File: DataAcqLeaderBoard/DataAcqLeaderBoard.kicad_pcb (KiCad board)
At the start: 2 copper layers, 71 parts, among them J2 PER_CAN, J3 PER_PWR, J4 CCAN_IN, J5 CCAN_OUT, J6 PWR_IN, SW1 RF_RESET, SW2 RF_COM, SW3 LTE_RESET, SW4 GPS_RESET, U1 PA1616S_GPS, X1 DigiXBeeRX900Micro, X2 DigiXBee3LTECat4

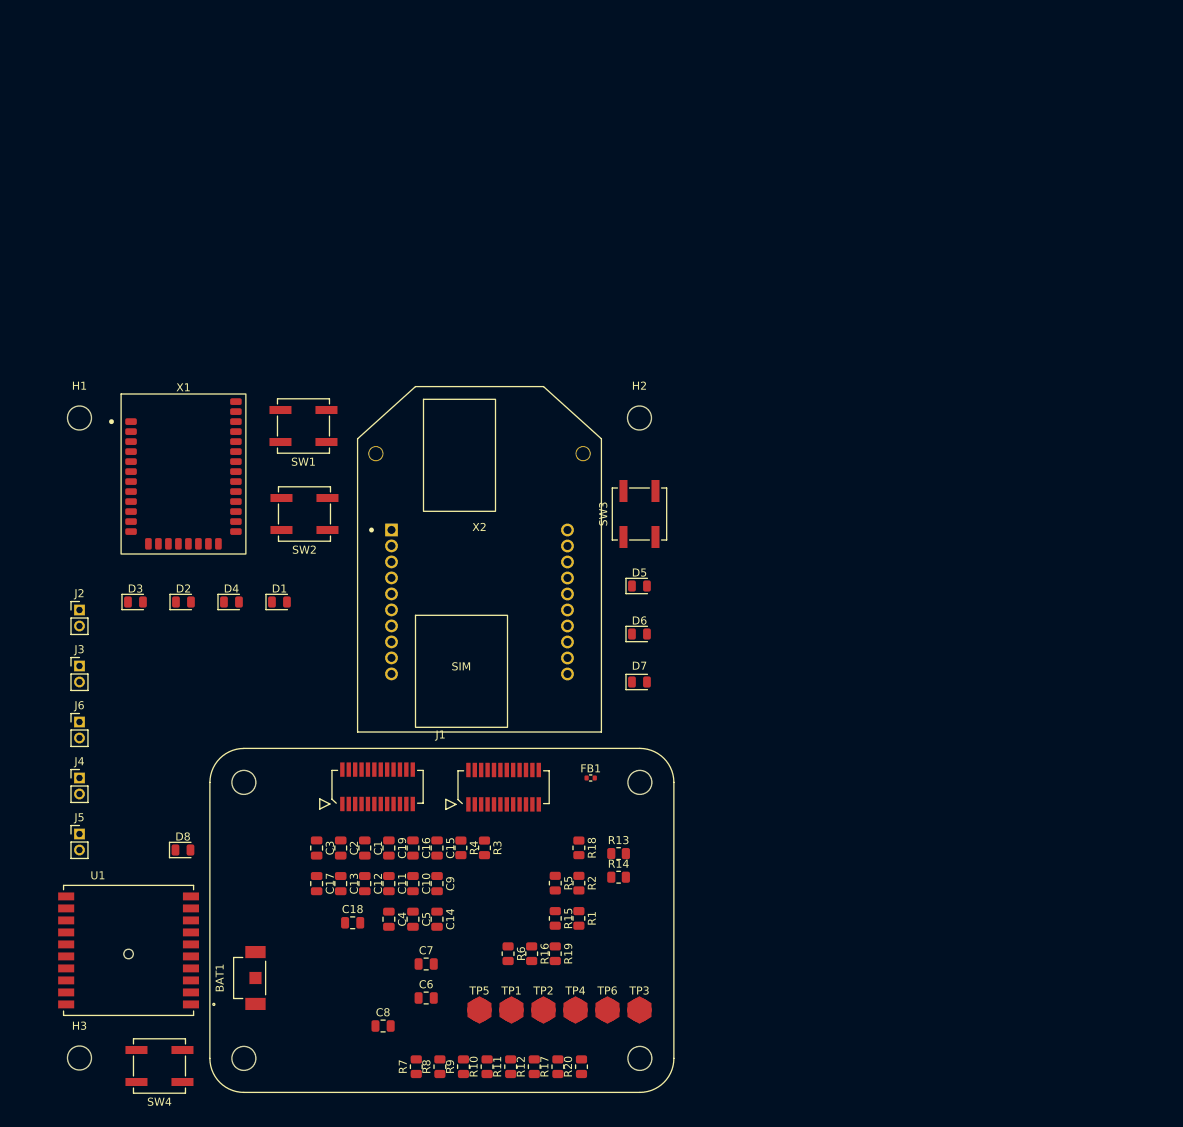
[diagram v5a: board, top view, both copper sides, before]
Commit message: Completed first draft of layout
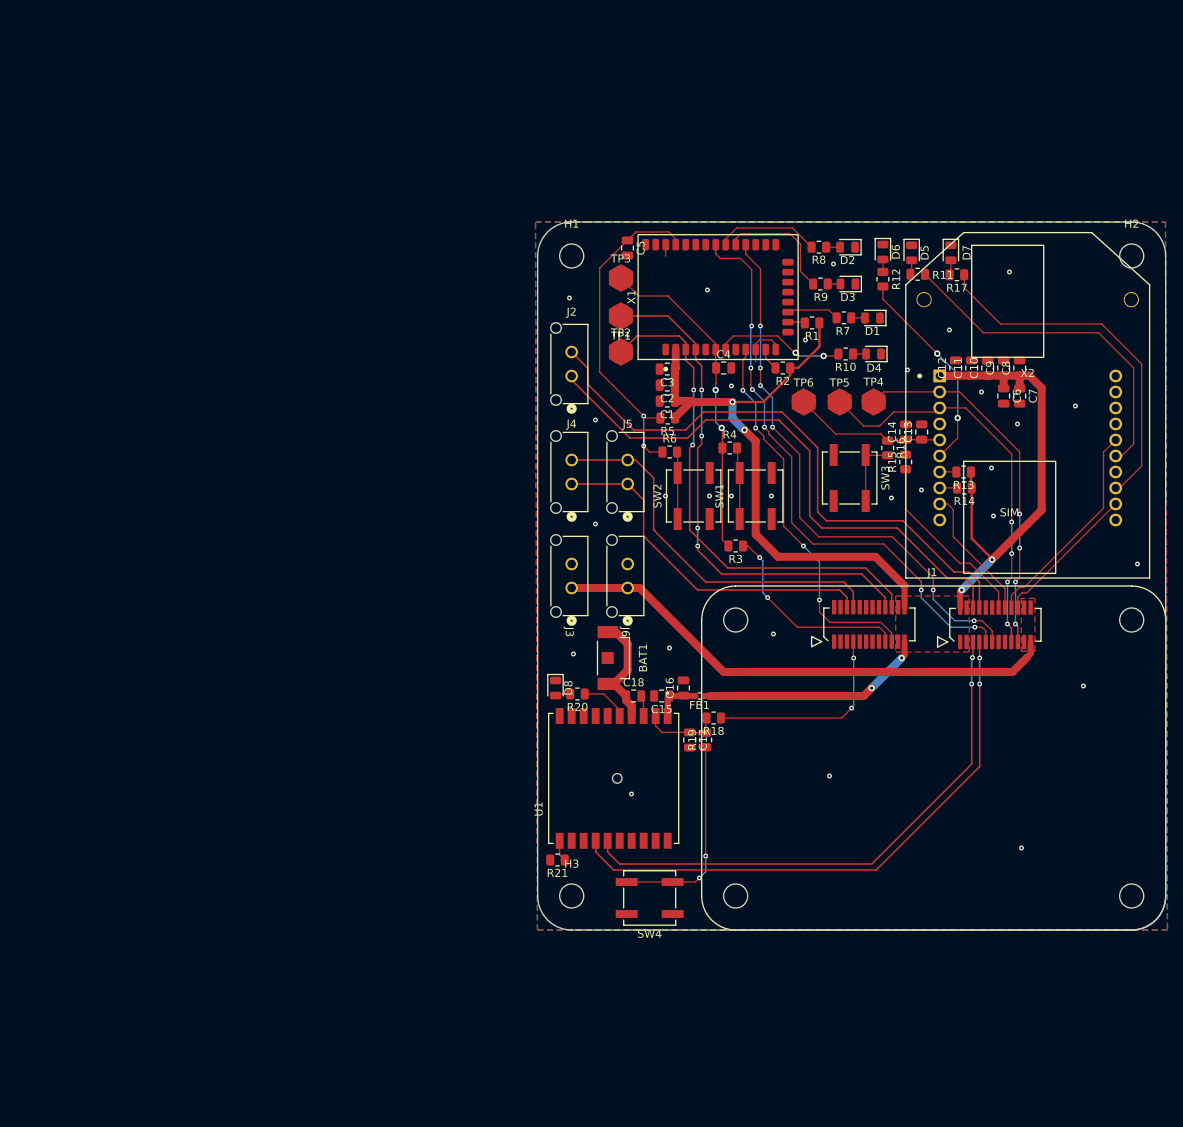
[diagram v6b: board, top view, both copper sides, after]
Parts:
- removed C19: 0.1u, Capacitor_SMD:C_0805_2012Metric
- added R21: 10k, Resistor_SMD:R_0805_2012Metric, F.Cu at (149.8, 135.2)
- J2, J3, J4, J5, J6: footprint Connector_PinHeader_2.00mm:PinHeader_1x02_P2.00mm_Vertical -> DataAcqLeaderBoard-Footprints:CONN_SD-43650-006_02_MOL
- moved C8 114.4 mm to (207.5, 73.8), turned to 90 degrees
- moved R8 112.9 mm to (182.4, 58.6), turned to 0 degrees
- moved R11 111.4 mm to (194.8, 62.0), turned to 180 degrees
- moved R17 110.8 mm to (199.7, 62.1), turned to 180 degrees
- moved R7 107.8 mm to (185.6, 67.5), turned to 0 degrees
- moved R12 107.7 mm to (190.4, 62.6)
- moved R9 107.5 mm to (182.6, 63.2), turned to 0 degrees
- moved C6 104.3 mm to (205.5, 77.2), turned to -90 degrees
- moved C7 102.7 mm to (207.5, 77.2), turned to -90 degrees
- moved R10 99.7 mm to (185.8, 72.0), turned to 0 degrees
- moved C12 98.0 mm to (199.5, 73.8), turned to 90 degrees
- moved D3 97.5 mm to (186.1, 63.2), turned to 180 degrees
- moved C11 97.3 mm to (201.5, 73.8), turned to 90 degrees
- moved C10 96.5 mm to (203.5, 73.8), turned to 90 degrees
- moved C9 95.8 mm to (205.5, 73.8), turned to 90 degrees
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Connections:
- net /GPS_CoinBattery_Supply renamed /+3.3V_GPS_BAT
- net /GPS_VCC renamed /+3.3V_GPS
- net Net-(D1-A) renamed /RF_D1
- net Net-(D2-A) renamed /RF_D2
- net Net-(D3-A) renamed /RF_D3
- net Net-(D4-A) renamed /RF_D4
- net Net-(D5-A) renamed /LTE_D5
- net Net-(D6-A) renamed /LTE_D6
- net Net-(D7-A) renamed /LTE_D7
- net Net-(D8-A) renamed /GPS_D8
- net Net-(R16-Pad2) renamed /LTE_SW3
- net Net-(R19-Pad1) renamed /GPS_SW4
- net Net-(R4-Pad2) renamed /RF_SW1
- net Net-(R6-Pad2) renamed /RF_SW2
- net Net-(X1-SPI_N_SSEL/DIO17) renamed /RF_SPI_OFF
- net Net-(X2-PWM1/DIO11/USB_D+/I2C_SDA) renamed /LTE_D+_OFF
- net Net-(X2-USB_D-) renamed /LTE_D-_OFF
- J1 pad 11: /RF_NRESET_MCU -> /RF_NCTS
- J1 pad 14: /LTE_NCTS -> /LTE_NRESET_MCU
- J1 pad 16: /LTE_NRTS -> /LTE_NDTR/SLEEP_RQ
- J1 pad 18: /LTE_NRESET_MCU -> /LTE_NRTS
- J1 pad 20: /LTE_NDTR/SLEEP_RQ -> /LTE_NCTS
- J1 pad 31: /GPS_NRESET -> /GPS_NRESET_MCU
- J1 pad 41: /RF_NRTS -> /RF_NRESET_MCU
- J1 pad 43: /RF_NCTS -> /RF_SLEEP
- J1 pad 9: /RF_SLEEP -> /RF_NRTS
- R18 pad 1: /GPS_NRESET -> /GPS_NRESET_MCU
- U1 pad 11: Net-(U1-EX_ANT) -> /GPS_EXT_OFF
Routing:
- net +3.3V: track 0.00 -> 164.9 mm, vias 0 -> 6
- net /CAN_PERF_L: track 0.00 -> 73.8 mm
- net /RF_NRTS: track 0.00 -> 72.7 mm, vias 0 -> 6
- net /GPS_I2C_SCL: track 0.00 -> 71.3 mm, vias 0 -> 2
- net /CAN_PERF_H: track 0.00 -> 70.7 mm
- net /RF_NCTS: track 0.00 -> 69.8 mm, vias 0 -> 6
- net /GPS_I2C_SDA: track 0.00 -> 68.0 mm, vias 0 -> 2
- net /RF_UART_TX: track 0.00 -> 64.3 mm, vias 0 -> 2
- net /RF_UART_RX: track 0.00 -> 64.2 mm, vias 0 -> 4
- net +12V: track 0.00 -> 64.1 mm
- net /LTE_UART_RX: track 0.00 -> 50.0 mm, vias 0 -> 4
- net /RF_SLEEP: track 0.00 -> 48.5 mm, vias 0 -> 4
- net /CAN_CAR_L: track 0.00 -> 47.8 mm
- net /LTE_UART_TX: track 0.00 -> 46.3 mm, vias 0 -> 4
- net /LTE_STATUS_ON: track 0.00 -> 44.9 mm
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- added copper zone on F.Cu, net +12V
- added copper zone on F.Cu, net +3.3V
- added copper zone on B.Cu, net GND
- added copper zone on F.Cu, net GND
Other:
- board outline added: 78.5 x 88.5 mm

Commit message: Updated Schematic, finished first rev of Layout
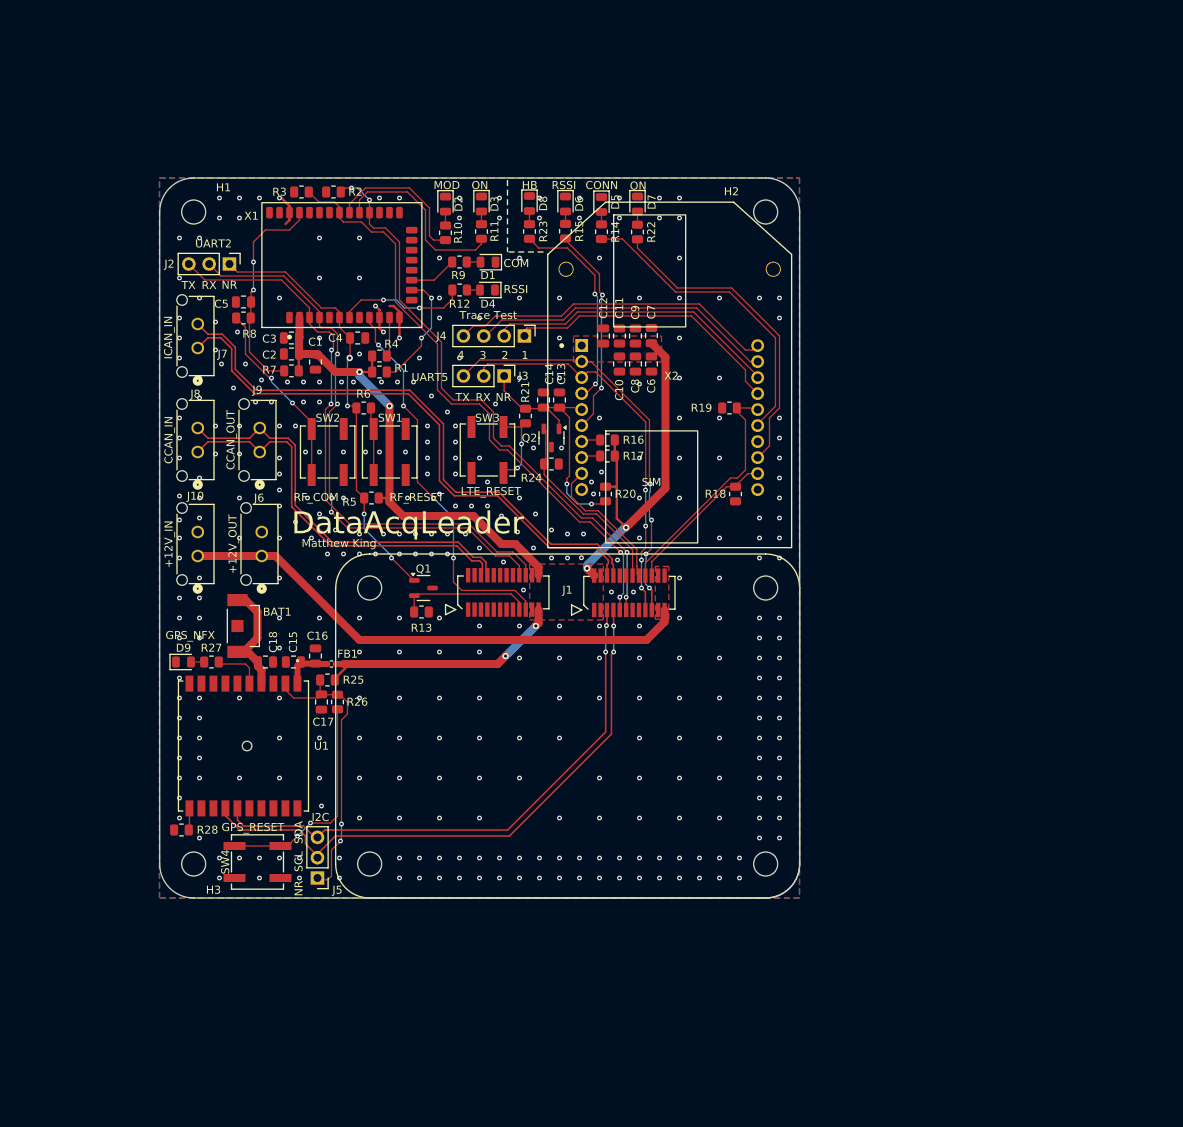
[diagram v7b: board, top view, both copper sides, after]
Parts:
- removed TP1: RF_UART_RX, UTSVT_Special:TestPoint_HEX_3mmID
- removed TP2: RF_UART_TX, UTSVT_Special:TestPoint_HEX_3mmID
- removed TP3: RF_NREST, UTSVT_Special:TestPoint_HEX_3mmID
- removed TP4: LTE_UART_TX, UTSVT_Special:TestPoint_HEX_3mmID
- removed TP5: LTE_UART_RX, UTSVT_Special:TestPoint_HEX_3mmID
- removed TP6: LTE_NRESET, UTSVT_Special:TestPoint_HEX_3mmID
- added D8: LTE_HeartBeat, LED_SMD:LED_0805_2012Metric, F.Cu at (146.2, 53.2)
- added J6: PWR_OUT, DataAcqLeaderBoard-Footprints:CONN_SD-43650-006_02_MOL, F.Cu at (112.5, 95.8)
- added J7: ICAN_IN, DataAcqLeaderBoard-Footprints:CONN_SD-43650-006_02_MOL, F.Cu at (104.5, 69.8)
- added J8: CCAN_IN, DataAcqLeaderBoard-Footprints:CONN_SD-43650-006_02_MOL, F.Cu at (104.5, 82.8)
- added J9: CCAN_OUT, DataAcqLeaderBoard-Footprints:CONN_SD-43650-006_02_MOL, F.Cu at (112.2, 82.8)
- added Q1: NMOS, Package_TO_SOT_SMD:SOT-23-3, F.Cu at (133.0, 101.2)
- added Q2: NMOS, Package_TO_SOT_SMD:SOT-23-3, F.Cu at (149.0, 82.5)
- added R13: 10k, Resistor_SMD:R_0805_2012Metric, F.Cu at (132.8, 104.2)
- added R18: 10k, Resistor_SMD:R_0805_2012Metric, F.Cu at (172.0, 89.5)
- added R19: 10k, Resistor_SMD:R_0805_2012Metric, F.Cu at (171.2, 78.8)
- added R2: 10k, Resistor_SMD:R_0805_2012Metric, F.Cu at (121.8, 51.8)
- added R23: 1k, Resistor_SMD:R_0805_2012Metric, F.Cu at (146.2, 56.7)
- added R24: 10k, Resistor_SMD:R_0805_2012Metric, F.Cu at (149.0, 85.8)
- added R3: 10k, Resistor_SMD:R_0805_2012Metric, F.Cu at (117.8, 51.8)
- J2: value PER_CAN -> RF_UART; footprint DataAcqLeaderBoard-Footprints:CONN_SD-43650-006_02_MOL -> Connector_PinHeader_2.54mm:PinHeader_1x03_P2.54mm_Vertical
- J3: value PER_PWR -> LTE_UART; footprint DataAcqLeaderBoard-Footprints:CONN_SD-43650-006_02_MOL -> Connector_PinHeader_2.54mm:PinHeader_1x03_P2.54mm_Vertical
- J4: value CCAN_IN -> LTE_Trace; footprint DataAcqLeaderBoard-Footprints:CONN_SD-43650-006_02_MOL -> Connector_PinHeader_2.54mm:PinHeader_1x04_P2.54mm_Vertical
- J5: value CCAN_OUT -> GPS_I2C; footprint DataAcqLeaderBoard-Footprints:CONN_SD-43650-006_02_MOL -> Connector_PinHeader_2.54mm:PinHeader_1x03_P2.54mm_Vertical
- R10: renamed from R8; value 700 -> 1k
- R11: renamed from R9; value 700 -> 1k
- R12: renamed from R10; value 700 -> 1k
- R14: renamed from R11; value 700 -> 1k
- R15: renamed from R12; value 700 -> 1k
- R21: renamed from R16; value 700 -> 1k
- R22: renamed from R17; value 700 -> 1k
- R26: renamed from R19; value 700 -> 1k
- R27: renamed from R20; value 700 -> 1k
- R6: renamed from R4; value 700 -> 1k
- R8: renamed from R6; value 700 -> 1k
- R9: renamed from R7; value 700 -> 1k
- moved J5 63.7 mm to (119.8, 137.5), turned to 180 degrees
- moved R8 55.8 mm to (110.5, 67.5), turned to 180 degrees
- moved R1 54.4 mm to (127.5, 74.2), turned to 0 degrees
- moved J10 53.9 mm to (104.5, 95.8)
- moved D2 50.6 mm to (135.8, 53.3), turned to -90 degrees
- moved R4 50.4 mm to (127.5, 72.2), turned to 0 degrees
- moved SW4 49.2 mm to (112.2, 135.5)
- moved D4 48.9 mm to (141.0, 64.0)
- moved R12 48.9 mm to (137.5, 64.0)
- moved D1 48.6 mm to (141.1, 60.5)
- moved R9 48.6 mm to (137.5, 60.5)
- moved R25 48.5 mm to (121.0, 112.8), turned to 0 degrees
- moved C5 48.5 mm to (110.5, 65.5), turned to 180 degrees
- moved C8 48.0 mm to (159.5, 73.2), turned to -90 degrees
- moved H1 47.6 mm to (104.3, 54.2)
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- renumbered D8 to D9, J6 to J10, R13 to R16, R14 to R17, R15 to R20, R18 to R25, R21 to R28, R2 to R4, R3 to R5, R5 to R7
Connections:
- net /GPS_D8 renamed /GPS_D9
- J1 pad 30: /CAN_CAR_H -> /CAN_CAR_+
- J1 pad 31: /GPS_NRESET_MCU -> unconnected-(J1B-ADC1_IN10-Pad31)
- J1 pad 32: /CAN_CAR_L -> /CAN_CAR_-
- J1 pad 6: /CAN_PERF_H -> /CAN_PERF_+
- J1 pad 8: /CAN_PERF_L -> /CAN_PERF_-
- J2 pad 1: /CAN_PERF_H -> /RF_NRESET
- J2 pad 2: /CAN_PERF_L -> /RF_UART_RX
- J3 pad 1: +12V -> /LTE_NRESET
- J3 pad 2: GND -> /LTE_UART_RX
- J4 pad 1: /CAN_CAR_H -> /LTE_Trace1
- J4 pad 2: /CAN_CAR_L -> /LTE_Trace2
- J5 pad 1: /CAN_CAR_H -> /GPS_NRESET
- J5 pad 2: /CAN_CAR_L -> /GPS_I2C_SCL
- R20 pad 1: /LTE_NRESET_MCU -> +3.3V
- R25 pad 1: /GPS_NRESET_MCU -> /GPS_NRESET
- R25 pad 2: /GPS_NRESET -> +3.3V
- R5 pad 1: /RF_NRESET_MCU -> +3.3V
- X2 pad 17: unconnected-(X2-AD3/DIO3/SPI_N_SS/CTS_2-Pad17) -> /LTE_Trace1
- X2 pad 18: unconnected-(X2-AD2/DIO2/SPI_CLK/RTS_2-Pad18) -> /LTE_Trace2
- X2 pad 19: unconnected-(X2-AD1/DIO1/SPI_N_ATTN/I2C_SCL-Pad19) -> /LTE_Trace3
- X2 pad 20: unconnected-(X2-AD0/DIO0-Pad20) -> /LTE_Trace4
- X2 pad 4: unconnected-(X2-DIO12/SPI_MISO/UART_RX2-Pad4) -> /LTE_STATUS_HB
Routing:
- net /CAN_PERF_L: track 73.8 -> 0.00 mm
- net /CAN_PERF_-: track 0.00 -> 72.1 mm
- net /CAN_PERF_+: track 0.00 -> 71.9 mm
- net /CAN_PERF_H: track 70.7 -> 0.00 mm
- net /CAN_CAR_-: track 0.00 -> 50.1 mm
- net /CAN_CAR_+: track 0.00 -> 49.4 mm
- net /CAN_CAR_L: track 47.8 -> 0.00 mm
- net /CAN_CAR_H: track 44.2 -> 0.00 mm
- net /LTE_Trace4: track 0.00 -> 41.0 mm
- net /LTE_Trace3: track 0.00 -> 38.5 mm
- net /LTE_Trace2: track 0.00 -> 36.9 mm
- net /LTE_Trace1: track 0.00 -> 35.6 mm
- net /LTE_STATUS_HB: track 0.00 -> 26.1 mm, vias 0 -> 2
- net /GPS_NRESET: track 10.2 -> 35.9 mm, vias 0 -> 2
- net /GPS_NRESET_MCU: track 25.3 -> 0.00 mm, vias 2 -> 0
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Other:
- board size 78.5 x 88.5 mm -> 80 x 90 mm
- board text added: "+12V_IN"
- board text added: "+12V_OUT"
- board text added: "1"
- board text added: "2"
- board text added: "3"
- board text added: "4"
- board text added: "CCAN_IN"
- board text added: "CCAN_OUT"
- board text added: "COM"
- board text added: "CONN"
- board text added: "DataAcqLeader"
- board text added: "GPS_NFX"
- board text added: "GPS_RESET"
- board text added: "HB"
- board text added: "I2C"
- board text added: "ICAN_IN"
- board text added: "LTE_RESET"
- board text added: "MOD"
- board text added: "Matthew King"
- board text added: "NR"
- board text added: "ON"
- board text added: "RF_COM"
- board text added: "RF_RESET"
- board text added: "RSSI"
- board text added: "RX"
- board text added: "SCL"
- board text added: "SDA"
- board text added: "TX"
- board text added: "Trace Test"
- board text added: "UART2"
- board text added: "UART5"

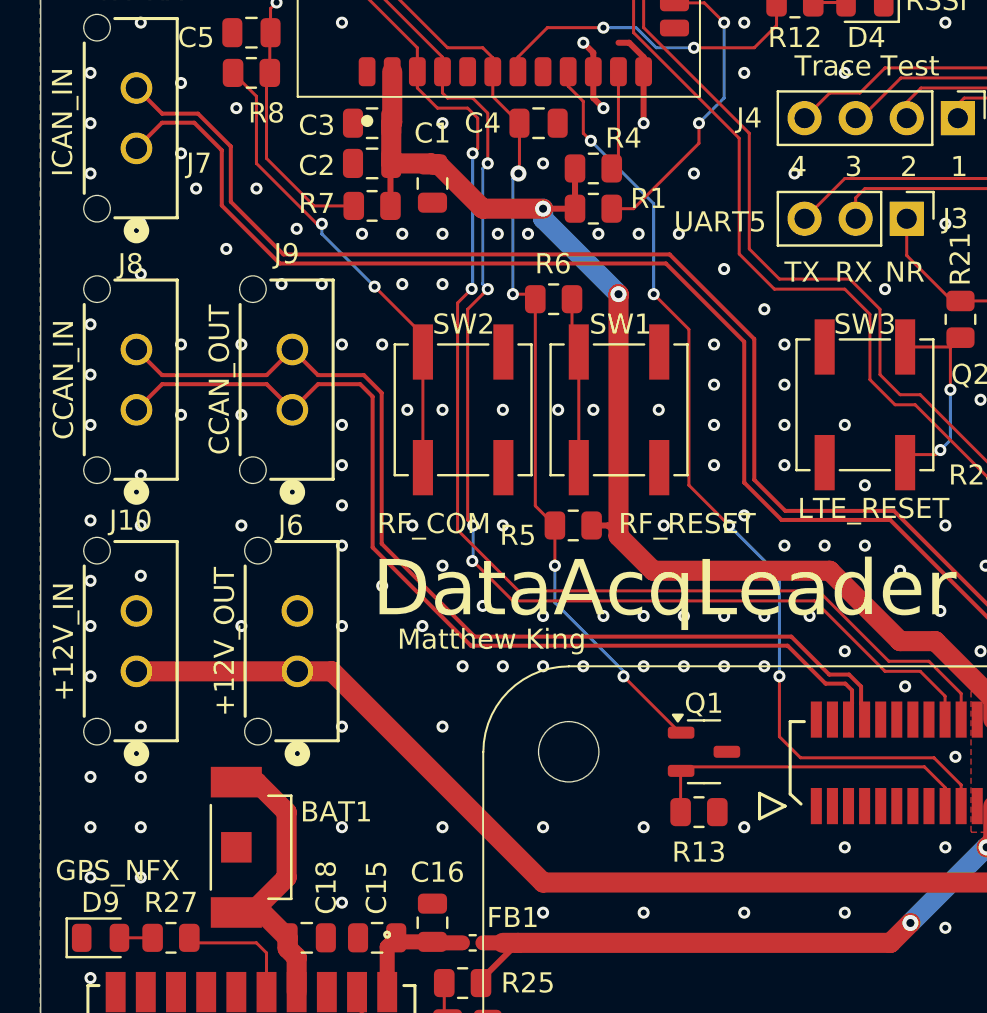
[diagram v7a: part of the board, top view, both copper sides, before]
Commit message: Added README, added PCB dimensions
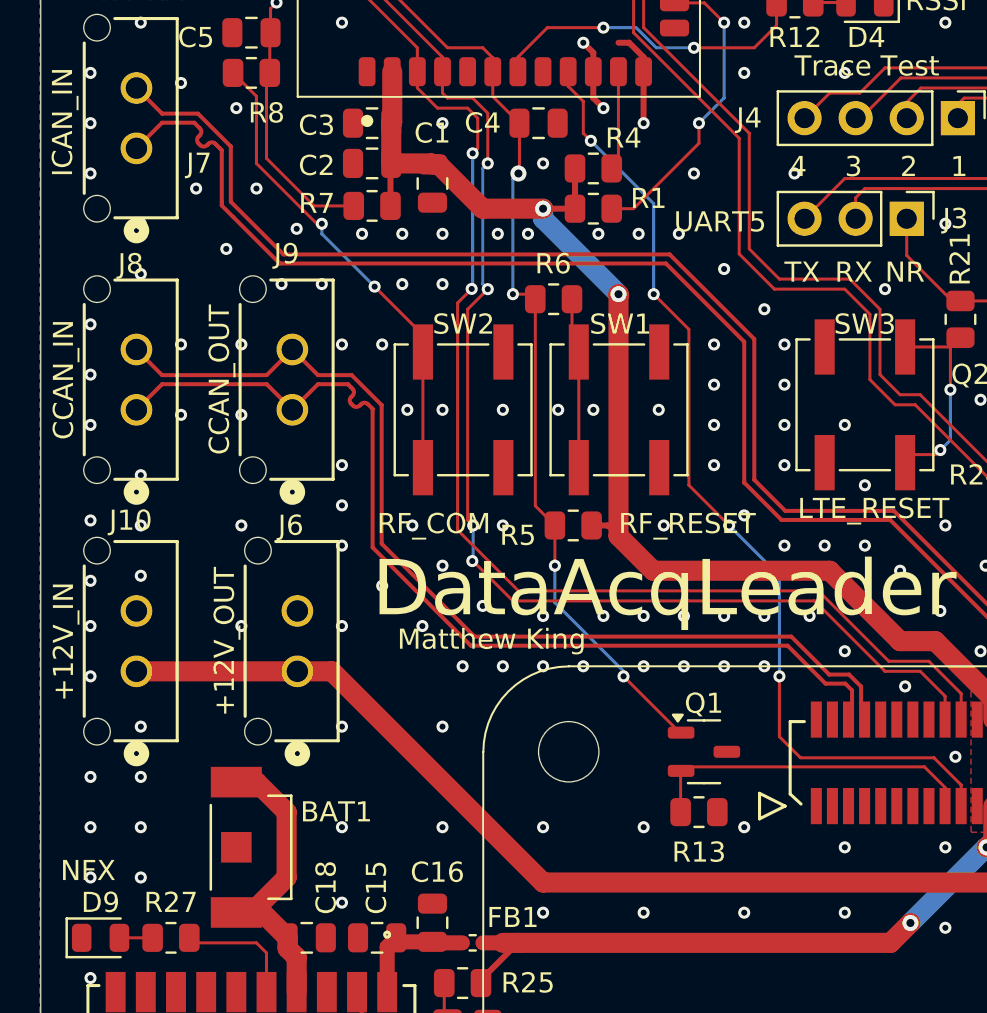
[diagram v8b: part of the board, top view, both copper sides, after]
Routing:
- net /CAN_PERF_+: track 71.9 -> 72.7 mm
- net GND: vias 358 -> 356
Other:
- board text added: "NFX"
- board text removed: "GPS_NFX"
